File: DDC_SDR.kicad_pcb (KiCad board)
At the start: 4 copper layers, 100 x 100 mm, 284 parts, among them J1 Filter, J10 SDR ANT, J11 Filter, J12 Filter, J2 S11, J3 Filter, J4 S21_OUT, J5 AWG_OUT, J6 PMOD, J7 Conn_01x02, J8 OLED, J9 3.5mm_Jack, Q1 2N7002, Q2 2N7002, Q3 AO3401A, Q4 2N7002, Q5 2N7002, Q6 2N7002, Q7 2N7002, Q8 2N7002, Q9 2N7002, SW1 RotaryEncoder_Switch_MP, U1 74LVC1G3157GW, U10 PAM8908, U11 NCP115AMX120TCG, U12 74LVC1G3157GW, U13 TPH2501-TR, U14 74LVC1G3157GW, U15 74LVC1G3157GW, U16 74LVC1G3157GW, U17 74LVC1G3157GW, U18 74LVC1G3157GW, U19 74LVC1G3157GW, U2 TPH2501-TR, U20 TPH2501-TR, U21 74LVC1G3157GW, U22 74LVC1G3157GW, U23 74LVC1G3157GW, U24 74LVC1G3157GW, U3 TPH2501-TR, U4 MS9280, U5 MS9708, U6 74LVC1G3157GW, U7 ICE40UP5K-SG48ITR, U8 L78M05ABDT-TR, U9 CJC4334H, X1 SG-8018CE 30.720000MHz TJHPA

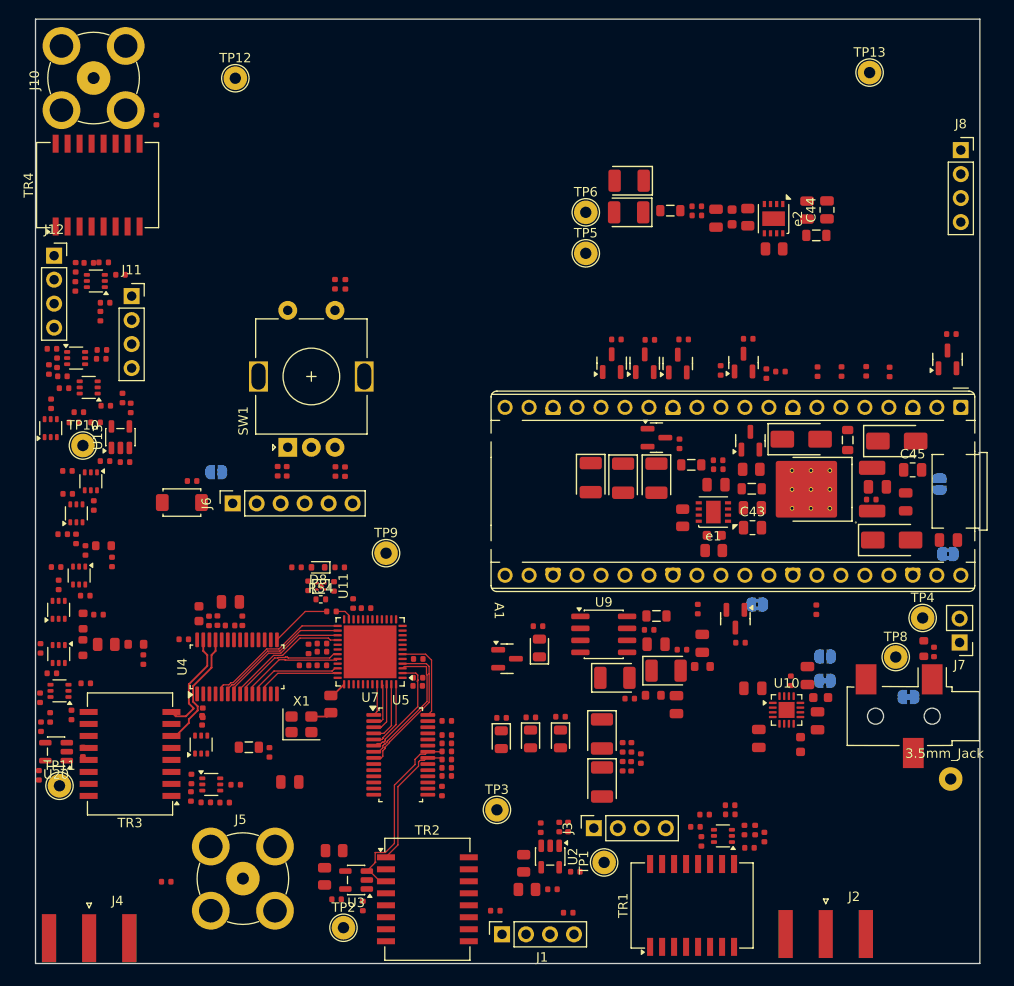
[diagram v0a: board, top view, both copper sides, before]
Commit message: Lots of signal traces wided
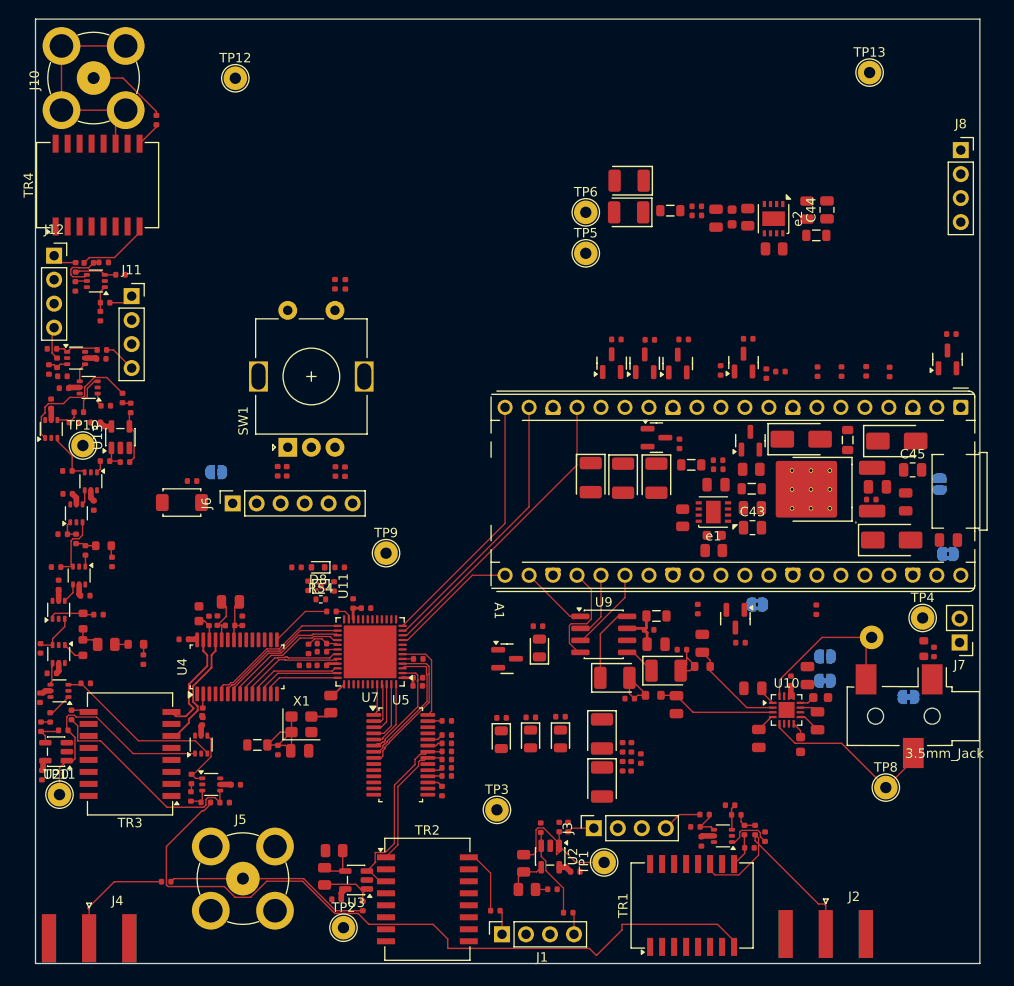
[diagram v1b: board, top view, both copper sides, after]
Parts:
- moved TP7 17.2 mm to (188.5, 115.5)
- moved TP8 13.9 mm to (190.0, 131.4)
- moved C55 3.46 mm to (128.0, 127.5)
- moved R80 3.09 mm to (102.9, 125.3), turned to 0 degrees
- moved TP11 0.94 mm to (102.5, 132.1)
- moved C56 0.93 mm to (125.7, 127.4)
- moved FB6 0.93 mm to (123.5, 126.9)
- moved C24 0.64 mm to (174.2, 134.3), turned to 180 degrees
- moved C93 0.32 mm to (100.7, 130.1)
- moved U12 0.11 mm to (101.7, 93.4)
- moved R20 0.08 mm to (177.2, 136.6)
- turned R2 to -90 degrees
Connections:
- C61 pad 1: Net-(U10-INR+) -> Net-(U10-INL+)
- C62 pad 1: Net-(U10-INL+) -> Net-(U10-INR+)
- J9 pad R: Net-(U10-OUTL) -> Net-(U10-OUTR)
- J9 pad S: Net-(e4-B) -> unconnected-(J9-PadS)
- J9 pad T: Net-(U10-OUTR) -> Net-(U10-OUTL)
- R49 pad 2: Net-(U10-INR+) -> Net-(U10-INL+)
- R50 pad 2: Net-(U10-INL+) -> Net-(U10-INR+)
- U7 pad 10: /RX_DATA -> /TX_DATA
- U7 pad 11: /BCK -> /RX_DATA
- U7 pad 12: /WS -> /BCK
- U7 pad 9: /TX_DATA -> /WS
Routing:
- net Net-(TR1-RD-): track 0.00 -> 79.0 mm
- net /TX_DATA: track 0.00 -> 32.0 mm
- net /RX_DATA: track 0.00 -> 29.4 mm
- net /BCK: track 0.00 -> 27.6 mm
- net Net-(R80-Pad2): track 0.00 -> 25.0 mm
- net Net-(J10-Ext): track 0.00 -> 24.4 mm
- net VDDA: track 0.00 -> 23.7 mm
- net Net-(J2-In): track 0.00 -> 23.2 mm
- net Net-(C3-Pad1): track 0.00 -> 22.8 mm
- net Net-(J5-In): track 0.00 -> 21.9 mm
- net Net-(U10-OUTR): track 0.00 -> 19.2 mm
- net Net-(U10-OUTL): track 0.00 -> 18.8 mm
- net Net-(R79-Pad2): track 0.00 -> 17.9 mm
- net Net-(R12-Pad2): track 0.00 -> 16.1 mm
- net Net-(C81-Pad1): track 0.00 -> 14.4 mm
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
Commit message: Routed SPI lines on the top
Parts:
- moved D6 13.2 mm to (183.3, 105.2)
- moved FB1 12.8 mm to (178.7, 105.1)
- moved R33 5.81 mm to (185.8, 93.1), turned to 0 degrees
- moved Q5 3.48 mm to (171.5, 86.4)
- moved R64 3.48 mm to (172.0, 83.9)
- moved R35 2.87 mm to (175.4, 87.5)
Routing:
- net /SPI0_RX: track 0.00 -> 67.5 mm
- net /SPI0_CLK: track 0.00 -> 66.2 mm
- net /SPI0_TX: track 0.00 -> 64.5 mm
- net Net-(A1-GPIO7): track 0.00 -> 3.20 mm
- net Net-(A1-GPIO6): track 0.00 -> 3.18 mm
- net Net-(A1-GPIO4): track 0.00 -> 2.51 mm

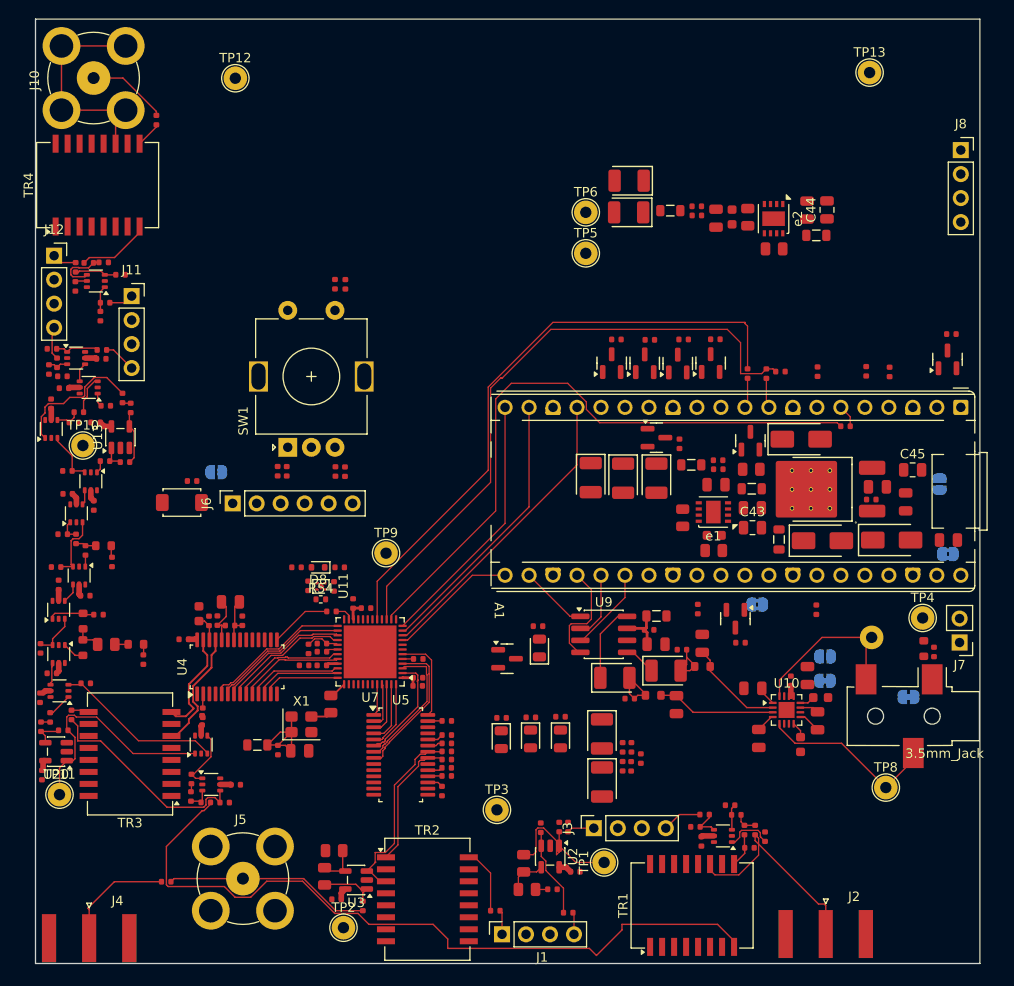
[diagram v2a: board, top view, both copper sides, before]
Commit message: PAM and LEDs
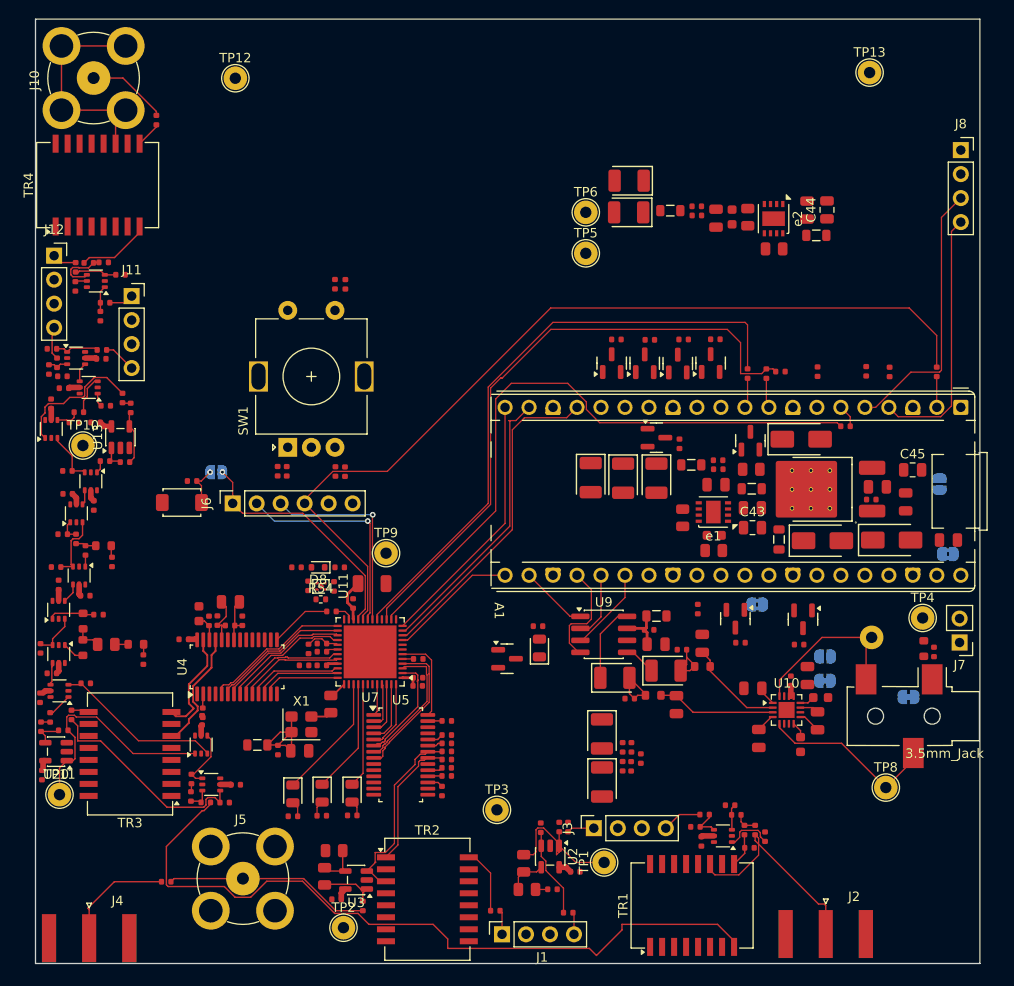
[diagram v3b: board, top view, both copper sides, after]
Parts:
- removed C30: 4.7uF, PCM_JLCPCB:C_0402
- added C107: 4.7uF, PCM_JLCPCB:C_1206, F.Cu at (135.6, 109.8)
- moved R88 36.6 mm to (180.9, 116.2), turned to 0 degrees
- moved Q9 31.5 mm to (181.3, 113.5), turned to -90 degrees
- moved R32 28.2 mm to (195.4, 87.3)
- moved R26 24.5 mm to (130.3, 134.3)
- moved R25 24.4 mm to (127.3, 134.4)
- moved R27 24.4 mm to (133.5, 134.3)
- moved D2 22.8 mm to (130.3, 132.0)
- moved D3 22.8 mm to (133.5, 132.0)
- moved D1 22.8 mm to (127.2, 132.0)
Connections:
- A1 pad 2: /~{T}/R -> Net-(A1-GPIO1)
- A1 pad 34: Net-(A1-GPIO28_ADC2) -> /~{T}/R
- J9 pad S: unconnected-(J9-PadS) -> Net-(e4-B)
- R32 pad 1: Net-(A1-GPIO28_ADC2) -> /PMOD_3
- R32 pad 2: /PMOD_3 -> Net-(A1-GPIO1)
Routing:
- net /PMOD_3: track 0.00 -> 95.5 mm
- net /SCL: track 0.00 -> 28.8 mm
- net /SDA: track 0.00 -> 27.4 mm
- net /PMOD_0: track 0.00 -> 25.9 mm, vias 0 -> 1
- net /PMOD_1: track 0.00 -> 23.2 mm, vias 0 -> 1
- net /PMOD_2: track 0.00 -> 21.3 mm, vias 0 -> 1
- net /RED: track 0.00 -> 13.3 mm
- net /YELLOW: track 0.00 -> 12.2 mm
- net /GREEN: track 0.00 -> 11.1 mm
- net Net-(JP2-B): track 0.00 -> 4.28 mm, vias 0 -> 1
- net Net-(A1-GPIO1): track 0.00 -> 3.26 mm
- net /TX_DATA: track 32.0 -> 34.7 mm
- net +3V3: track 8.37 -> 10.8 mm
- net Net-(D2-Pad2): track 0.00 -> 1.67 mm
- net Net-(D1-Pad2): track 0.00 -> 1.64 mm
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
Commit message: Added test points
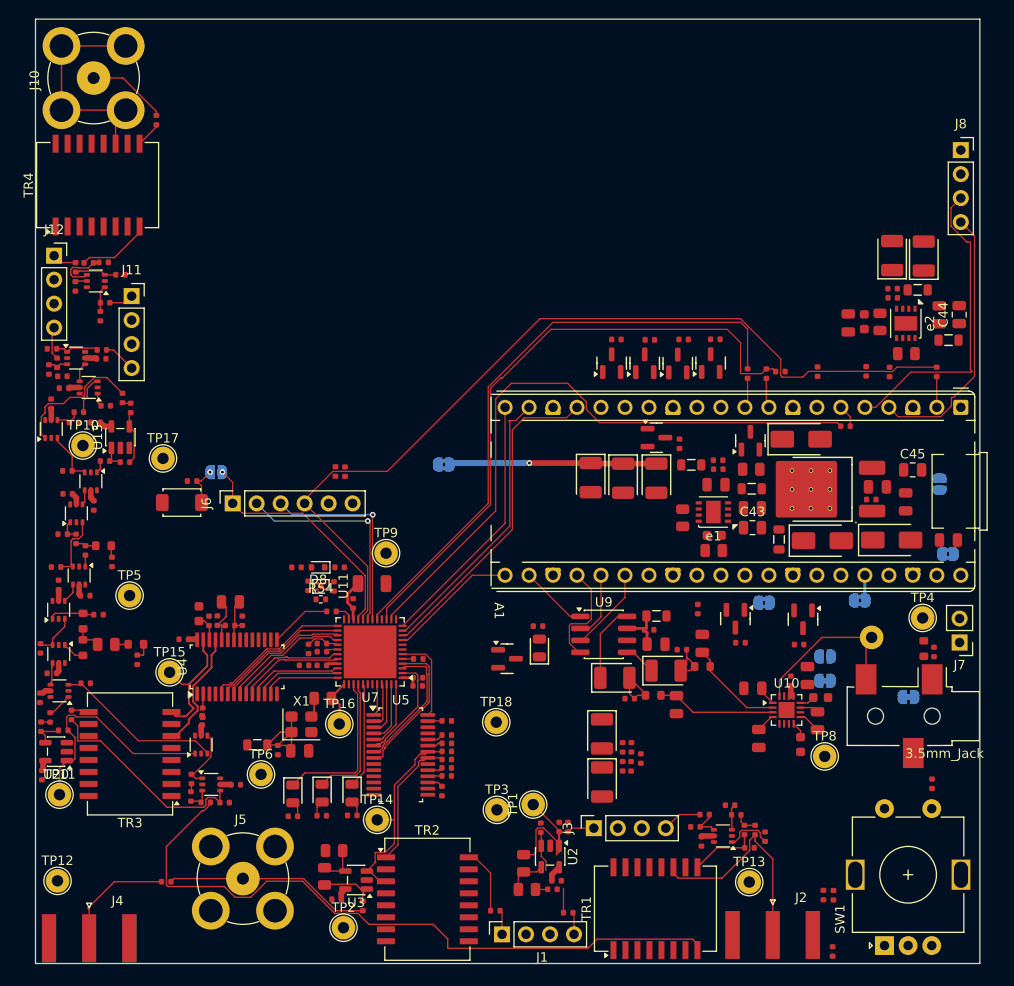
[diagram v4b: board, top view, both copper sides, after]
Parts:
- added JP7: VDDA, Jumper:SolderJumper-2_P1.3mm_Bridged2Bar_RoundedPad1.0x1.5mm, B.Cu at (143.2, 97.2)
- added JP8: +3V3, Jumper:SolderJumper-2_P1.3mm_Bridged2Bar_RoundedPad1.0x1.5mm, B.Cu at (187.3, 111.6)
- added TP14: U15, TestPoint:TestPoint_THTPad_D2.5mm_Drill1.2mm, F.Cu at (136.2, 134.8)
- added TP15: U15, TestPoint:TestPoint_THTPad_D2.5mm_Drill1.2mm, F.Cu at (114.2, 119.2)
- added TP16: U15, TestPoint:TestPoint_THTPad_D2.5mm_Drill1.2mm, F.Cu at (132.2, 124.6)
- added TP17: GND, TestPoint:TestPoint_THTPad_D2.5mm_Drill1.2mm, F.Cu at (113.5, 96.5)
- added TP18: GND, TestPoint:TestPoint_THTPad_D2.5mm_Drill1.2mm, F.Cu at (148.8, 124.5)
- moved C80 88.1 mm to (184.4, 148.7)
- moved TP12 87.1 mm to (102.3, 141.2)
- moved TP13 86.7 mm to (175.6, 141.4)
- moved SW1 82.3 mm to (189.9, 148.1)
- moved R55 81.6 mm to (194.9, 131.0)
- moved C79 74.0 mm to (184.5, 142.8), turned to 90 degrees
- moved R56 72.4 mm to (183.4, 142.8), turned to -90 degrees
- moved TP6 68.7 mm to (123.9, 130.0)
- moved TP5 60.4 mm to (110.0, 111.0)
- moved C53 32.2 mm to (194.1, 75.1), turned to 90 degrees
- moved C51 28.3 mm to (190.7, 75.0), turned to 90 degrees
- moved FB5 27.5 mm to (193.4, 78.7), turned to 0 degrees
- moved R47 22.5 mm to (190.8, 79.5)
- moved R46 22.5 mm to (190.8, 78.5)
- moved C42 17.9 mm to (195.7, 81.3)
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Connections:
- A1 pad 36: +3V3 -> Net-(A1-3V3)
- C50 pad 1: VDDA -> Net-(JP7-A)
- C52 pad 1: VDDA -> Net-(JP7-A)
- C54 pad 1: VDDA -> Net-(JP7-A)
- FB4 pad 2: VDDA -> Net-(JP7-A)
- TP5 pad 1: VDDA -> Net-(JP7-A)
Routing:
- net Net-(JP7-A): track 0.00 -> 22.1 mm, vias 0 -> 1
- net Net-(U10-OUTR): track 19.2 -> 0.00 mm
- net Net-(TR1-RD-): track 79.0 -> 73.0 mm
- net /SCL: track 28.8 -> 32.8 mm
- net Net-(TR1-RX-): track 3.58 -> 7.26 mm
- net /RED: track 13.3 -> 16.9 mm
- net /CLK: track 1.90 -> 5.32 mm
- net Net-(A1-3V3): track 0.00 -> 2.72 mm
- net Net-(U2-+): track 9.50 -> 6.85 mm
- net /A+: track 11.3 -> 13.9 mm
- net /O+: track 20.4 -> 22.2 mm
- net /YELLOW: track 12.2 -> 13.9 mm
- net /SDA: track 27.4 -> 28.7 mm
- net /PMOD_3: track 95.5 -> 94.6 mm
- net Net-(C89-Pad1): track 1.13 -> 1.79 mm
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
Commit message: Added Prototype Area
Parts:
- added REF**: Prototype_array, RP2040_minimal:Prototype_array, F.Cu at (144.6, 66.1)
- TP1, TP10, TP11, TP12, TP13, TP14, TP15, TP16, TP17, TP18, TP2, TP3, TP4, TP5, TP6, TP7, TP8, TP9: footprint TestPoint:TestPoint_THTPad_D2.5mm_Drill1.2mm -> RP2040_minimal:TestPoint_THTPad_D2.5mm_Drill1.2mm

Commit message: Some 3D models
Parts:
- moved REF** 5.27 mm to (149.7, 64.5)
